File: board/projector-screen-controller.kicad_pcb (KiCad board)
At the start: 2 copper layers, 97.2 x 106 mm, 60 parts, among them J1 ICSP, J2 MSTBVA-3-G, J3 MCV-3-G, J4 MCV-3-G, J5 MCV-3-G, J6 MSTBVA-6-G, J7 MCV-3-G, K1 JS1-12V-F, K2 JS1-12V-F, K3 JS1-12V-F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

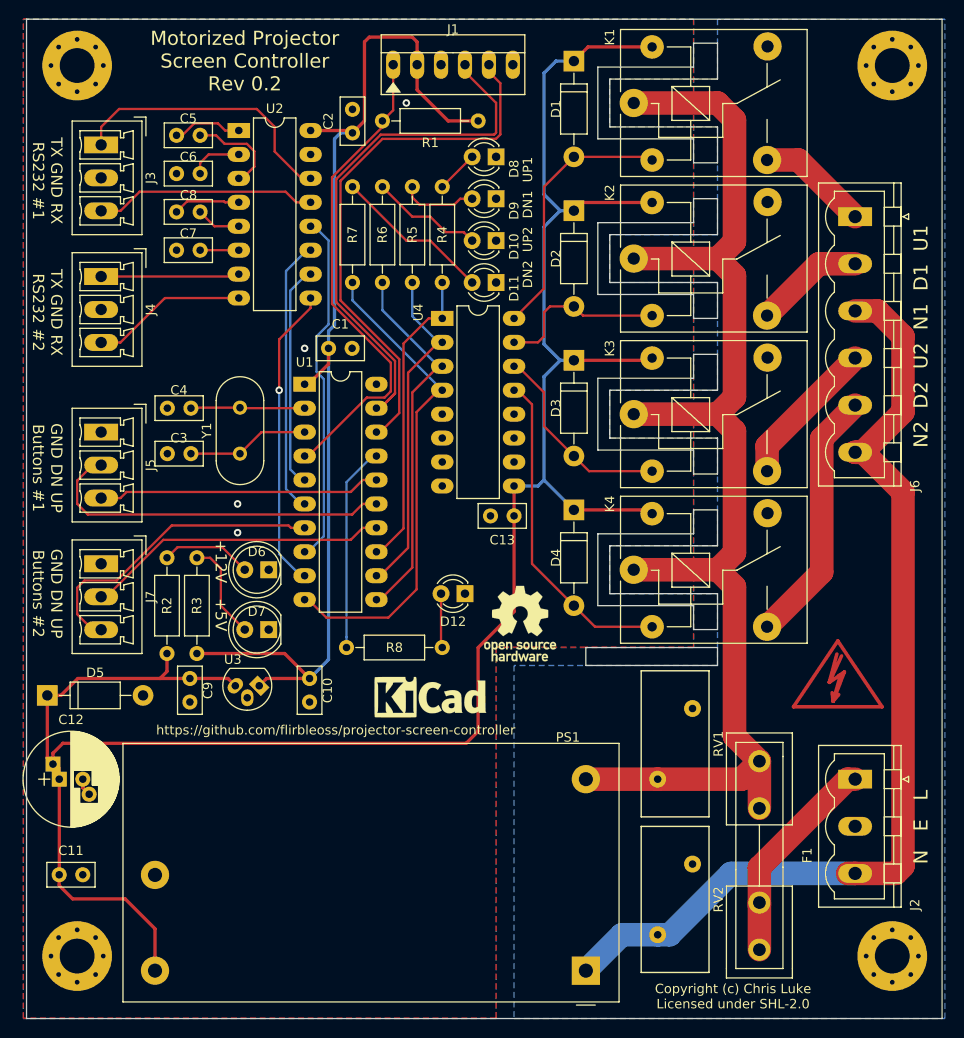
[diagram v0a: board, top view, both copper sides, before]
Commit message: Split the 5v and 12v ground paths
* To control the return path for (noisy) relay current, split the grounds for
  the 12v and 5v sections.
* The grounds are joined by bridges (solder pads) placed adjacent to the 5v
  regulator, on both layers.
* The gound plane is split in two; conveniently the 12v vs 5v components were
  already well placed to make this straightforward.
* 12v power LED uses the 5v ground to simplify routing.
* Add dummy power flags for ERC
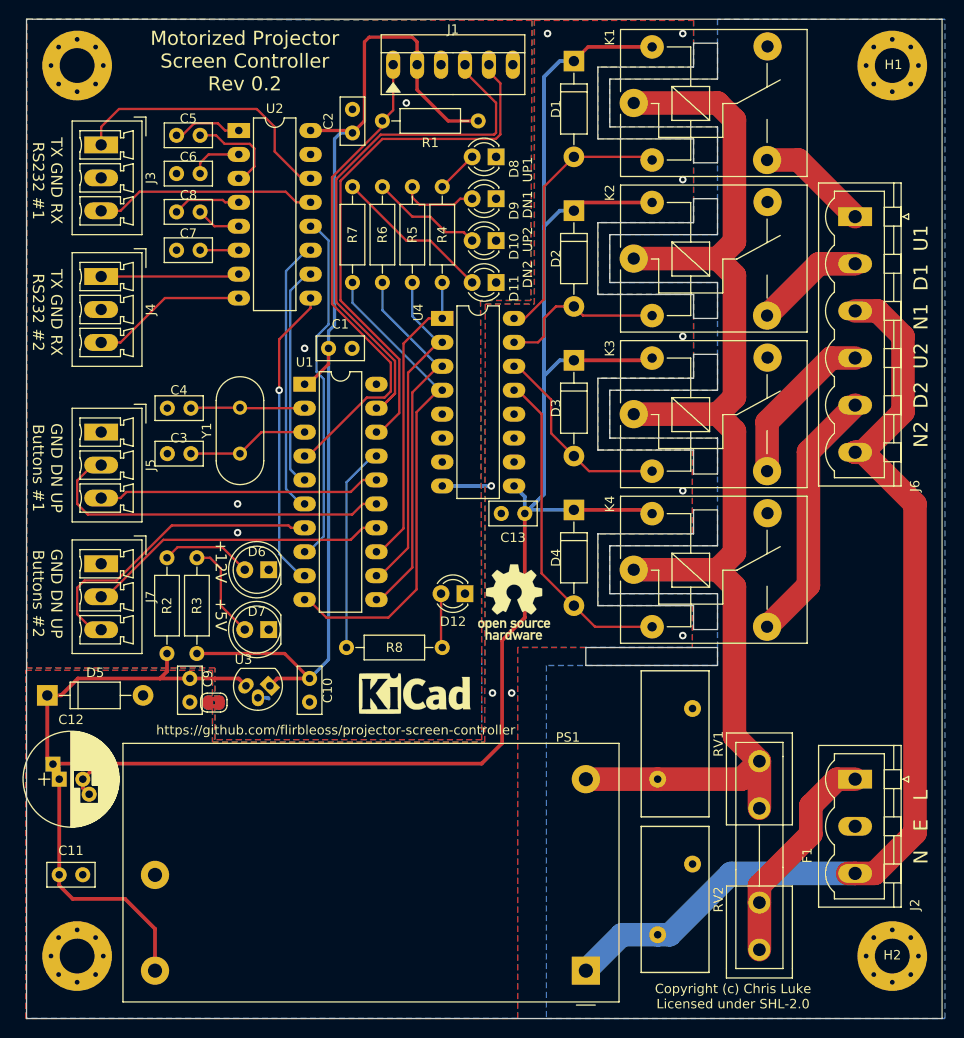
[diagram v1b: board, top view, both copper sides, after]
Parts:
- removed the REF** at (160.7, 115.3)
- removed the REF** at (166.5, 144.5)
- removed the REF** at (166.5, 50.0)
- added H1: MountingHole_Pad, Mounting_Holes:MountingHole_3.7mm_Pad_Via, F.Cu at (166.5, 50.0)
- added H2: MountingHole_Pad, Mounting_Holes:MountingHole_3.7mm_Pad_Via, F.Cu at (166.5, 144.5)
- added JP1: SolderJumper_2_Bridged, Jumper:SolderJumper-2_P1.3mm_Bridged2Bar_RoundedPad1.0x1.5mm, F.Cu at (94.5, 117.6)
- added JP2: SolderJumper_2_Bridged, Jumper:SolderJumper-2_P1.3mm_Bridged2Bar_RoundedPad1.0x1.5mm, B.Cu at (94.5, 117.6)
- moved REF*** 2.37 mm to (126.4, 106.9)
- moved REF** 1.69 mm to (115.8, 116.5)
- moved C13 1.17 mm to (127.5, 97.5)
- moved U3 1.13 mm to (100.5, 115.8)
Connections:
- C11 pad 2: GND -> GNDPWR
- C12 pad 2: GND -> GNDPWR
- C13 pad 2: GND -> GNDPWR
- C9 pad 2: GND -> GNDPWR
- D5 pad 2: GND -> GNDPWR
- PS1 pad 3: GND -> GNDPWR
- U4 pad 8: GND -> GNDPWR
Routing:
- net GNDPWR: track 0.00 -> 8.94 mm, vias 0 -> 9
- net +12V: track 230.7 -> 239.0 mm
- net /Relay/D2_UP_AC: track 15.9 -> 17.4 mm
- net +5V: track 118.0 -> 116.9 mm
- net /MCU/D2_UP_TTL: track 39.9 -> 39.1 mm
- net /MCU/D1_DN_TTL: track 36.4 -> 35.6 mm
- net GND: track 3.68 -> 2.99 mm
- net Net-(D1-Pad2): track 28.2 -> 28.9 mm
- net /MCU/D2_DN_TTL: track 51.8 -> 51.3 mm
- added copper zone on B.Cu, net GNDPWR
- added copper zone on F.Cu, net GNDPWR
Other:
- net class DC 12V added: clearance 0.2, trace_width 0.4, via_dia 0.8, via_drill 0.4
- net class DC 5V added: clearance 0.2, trace_width 0.35, via_dia 1, via_drill 0.5
- net class DC Power removed

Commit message: Add a smattering of ground vias
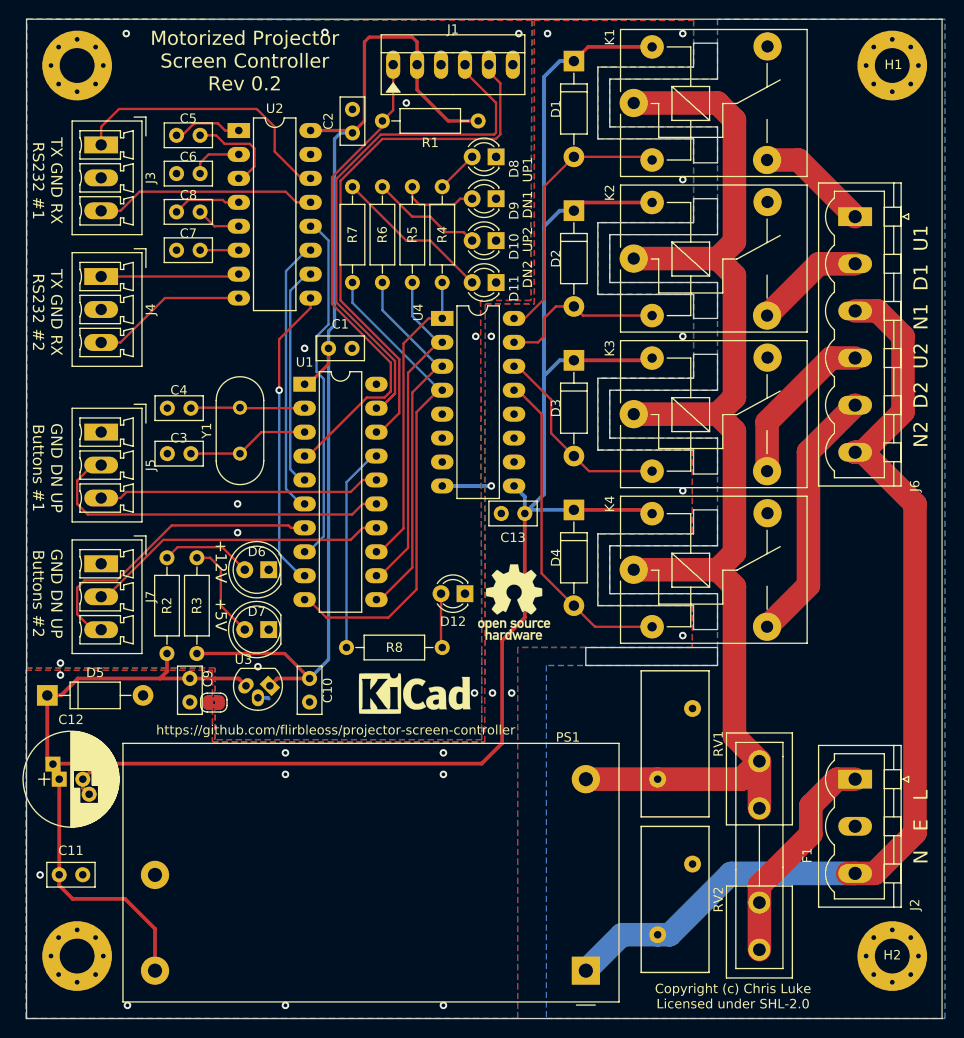
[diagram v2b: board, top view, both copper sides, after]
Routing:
- net GNDPWR: vias 9 -> 20
- net GND: vias 4 -> 11
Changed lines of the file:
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@@
     (thickness 1.6)
     (drawings 76)
-    (tracks 363)
+    (tracks 381)
     (zones 0)
     (modules 61)
@@
   )
   (setup
-    (last_trace_width 0.4)
+    (last_trace_width 0.25)
     (user_trace_width 0.35)
     (user_trace_width 0.4)
@@
   (segment (start 100.237 117.094) (end 100.33 117.187) (width 0.4) (layer B.Cu) (net 2))
   (segment (start 99.187 117.094) (end 100.237 117.094) (width 0.4) (layer B.Cu) (net 2))
+  (via (at 122.301 78.74) (size 0.8) (drill 0.4) (layers F.Cu B.Cu) (net 2))
+  (via (at 126.873 46.609) (size 0.8) (drill 0.4) (layers F.Cu B.Cu) (net 2))
+  (via (at 99.187 113.792) (size 0.8) (drill 0.4) (layers F.Cu B.Cu) (net 2))
+  (via (at 122.174 116.586) (size 0.8) (drill 0.4) (layers F.Cu B.Cu) (net 2))
+  (via (at 78.232 113.411) (size 0.8) (drill 0.4) (layers F.Cu B.Cu) (net 2))
+  (via (at 85.217 46.609) (size 0.8) (drill 0.4) (layers F.Cu B.Cu) (net 2))
+  (via (at 106.299 46.482) (size 0.8) (drill 0.4) (layers F.Cu B.Cu) (net 2))
   (segment (start 99.568 88.9) (end 97.282 91.186) (width 0.25) (layer F.Cu) (net 3) (status 20))
   (segment (start 104.14 88.9) (end 99.568 88.9) (width 0.25) (layer F.Cu) (net 3) (status 10))
@@
   (via (at 124.079 116.586) (size 0.8) (drill 0.4) (layers F.Cu B.Cu) (net 59))
   (via (at 123.952 94.615) (size 0.8) (drill 0.4) (layers F.Cu B.Cu) (net 59))
+  (via (at 102.108 122.936) (size 0.8) (drill 0.4) (layers F.Cu B.Cu) (net 59))
+  (via (at 102.108 125.222) (size 0.8) (drill 0.4) (layers F.Cu B.Cu) (net 59))
+  (via (at 118.872 122.936) (size 0.8) (drill 0.4) (layers F.Cu B.Cu) (net 59))
+  (via (at 118.872 125.222) (size 0.8) (drill 0.4) (layers F.Cu B.Cu) (net 59))
+  (via (at 123.952 78.74) (size 0.8) (drill 0.4) (layers F.Cu B.Cu) (net 59))
+  (via (at 82.55 122.936) (size 0.8) (drill 0.4) (layers F.Cu B.Cu) (net 59))
+  (via (at 78.232 114.681) (size 0.8) (drill 0.4) (layers F.Cu B.Cu) (net 59))
+  (via (at 76.073 135.89) (size 0.8) (drill 0.4) (layers F.Cu B.Cu) (net 59))
+  (via (at 118.872 149.733) (size 0.8) (drill 0.4) (layers F.Cu B.Cu) (net 59))
+  (via (at 102.108 149.733) (size 0.8) (drill 0.4) (layers F.Cu B.Cu) (net 59))
+  (via (at 85.344 149.733) (size 0.8) (drill 0.4) (layers F.Cu B.Cu) (net 59))
   (zone (net 0) (net_name "") (layers F&B.Cu) (hatch edge 0.508)
     (connect_pads (clearance 0.508))

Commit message: Update board symbols, minor ground plane fixes
* Fuse rating, board maximums
* ESD logo
* WEEE logo

* Some ground plane fixes around the MAX232
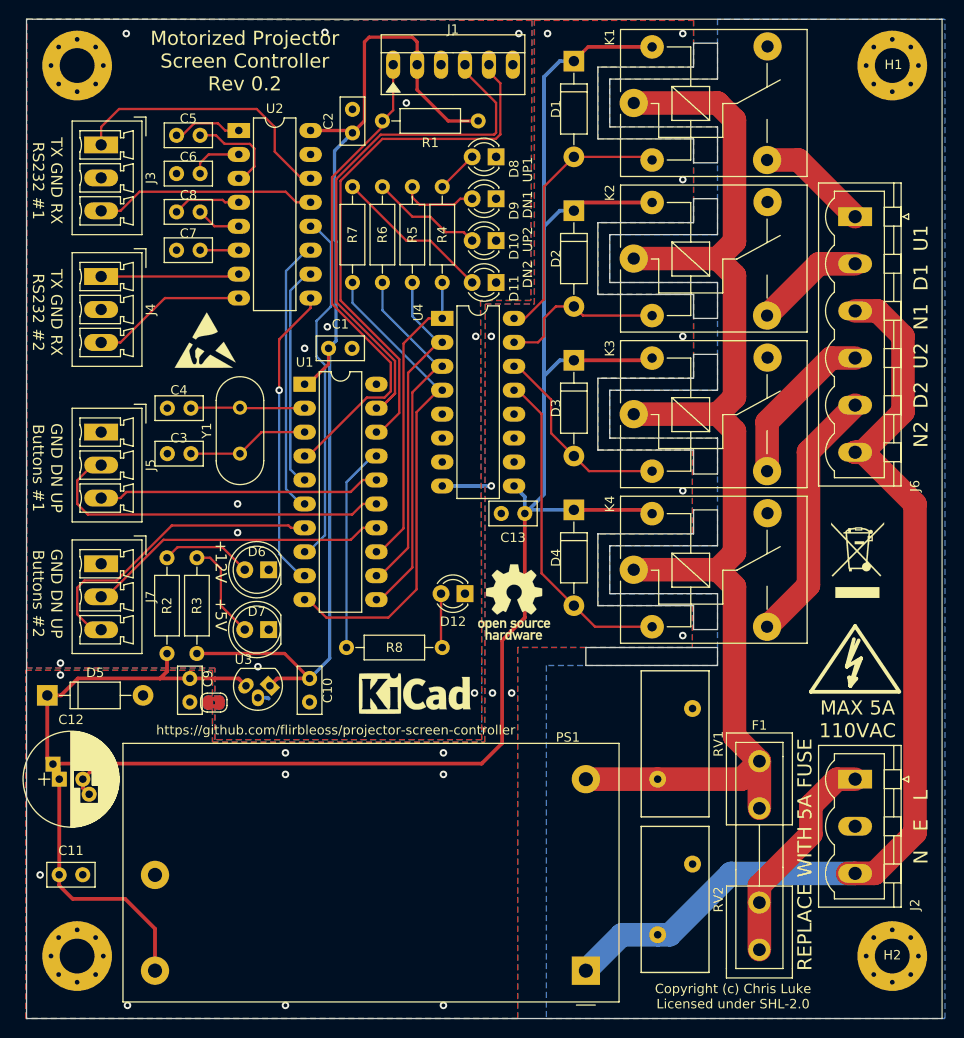
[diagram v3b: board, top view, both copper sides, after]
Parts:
- added REF***: WEEE-Logo_5.6x8mm_SilkScreen, Symbols:WEEE-Logo_5.6x8mm_SilkScreen, F.Cu at (162.8, 102.5)
- added REF***: ESD-Logo_6.6x6mm_SilkScreen, Symbols:ESD-Logo_6.6x6mm_SilkScreen, F.Cu at (93.6, 79.1)
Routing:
- net +5V: track 116.9 -> 116.4 mm
- net GND: vias 11 -> 12
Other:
- board text added: "MAX 5A 110VAC"
- board text added: "REPLACE WITH 5A FUSE"

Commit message: Fix KiCad 4 footprints
* Update the Phoenix connectors with KiCad 5 footprints
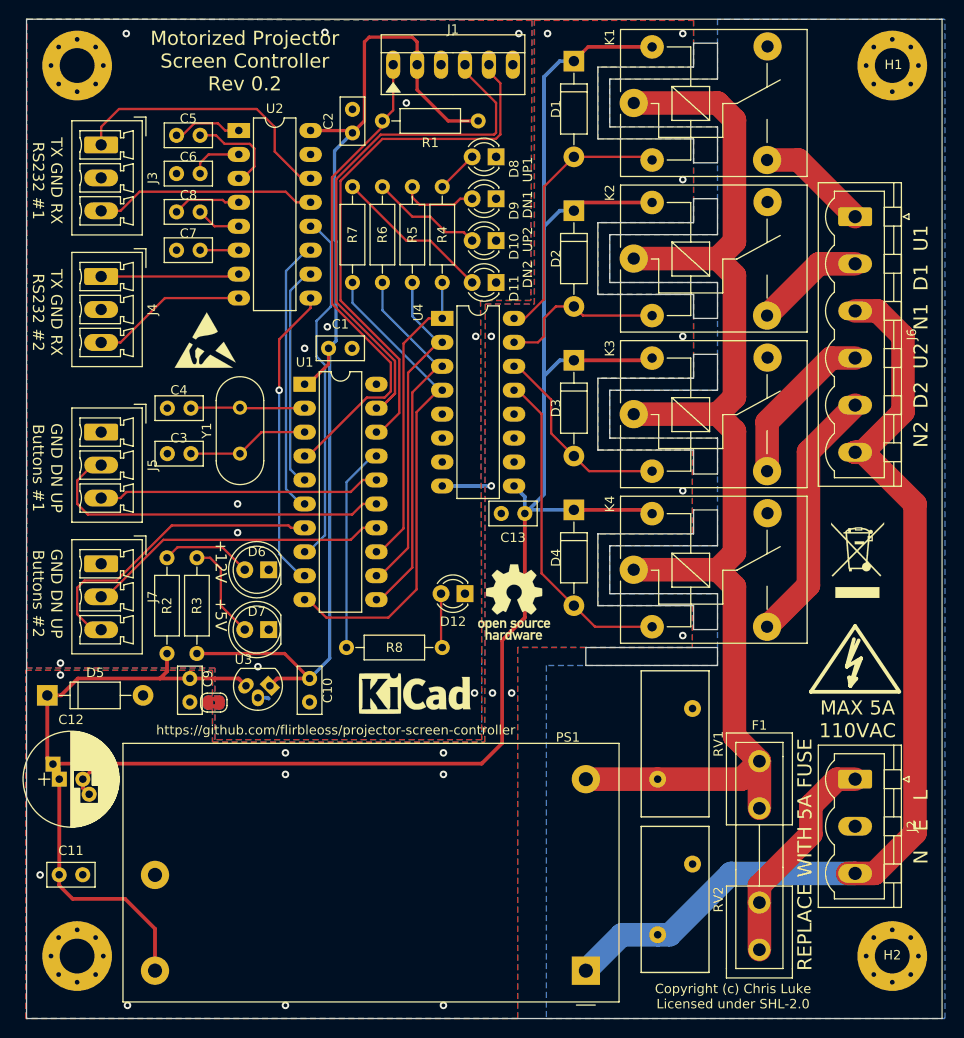
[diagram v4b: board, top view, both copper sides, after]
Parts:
- J2: footprint Connectors_Phoenix:PhoenixContact_MSTBVA-G_03x5.00mm_Vertical -> Connector_Phoenix_MSTB:PhoenixContact_MSTBVA_2,5_3-G_1x03_P5.00mm_Vertical
- J3, J4, J5, J7: footprint Connectors_Phoenix:PhoenixContact_MCV-G_03x3.50mm_Vertical -> Connector_Phoenix_MC:PhoenixContact_MCV_1,5_3-G-3.5_1x03_P3.50mm_Vertical
- J6: footprint Connectors_Phoenix:PhoenixContact_MSTBVA-G_06x5.00mm_Vertical -> Connector_Phoenix_MSTB:PhoenixContact_MSTBVA_2,5_6-G_1x06_P5.00mm_Vertical

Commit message: Update all footprints to KiCad 5 paths
* All footprints updated.
* 3D models for the relays seem to be missing from KiCad, however, so I
  have a copy in my personal library. Mostly cosmetic.
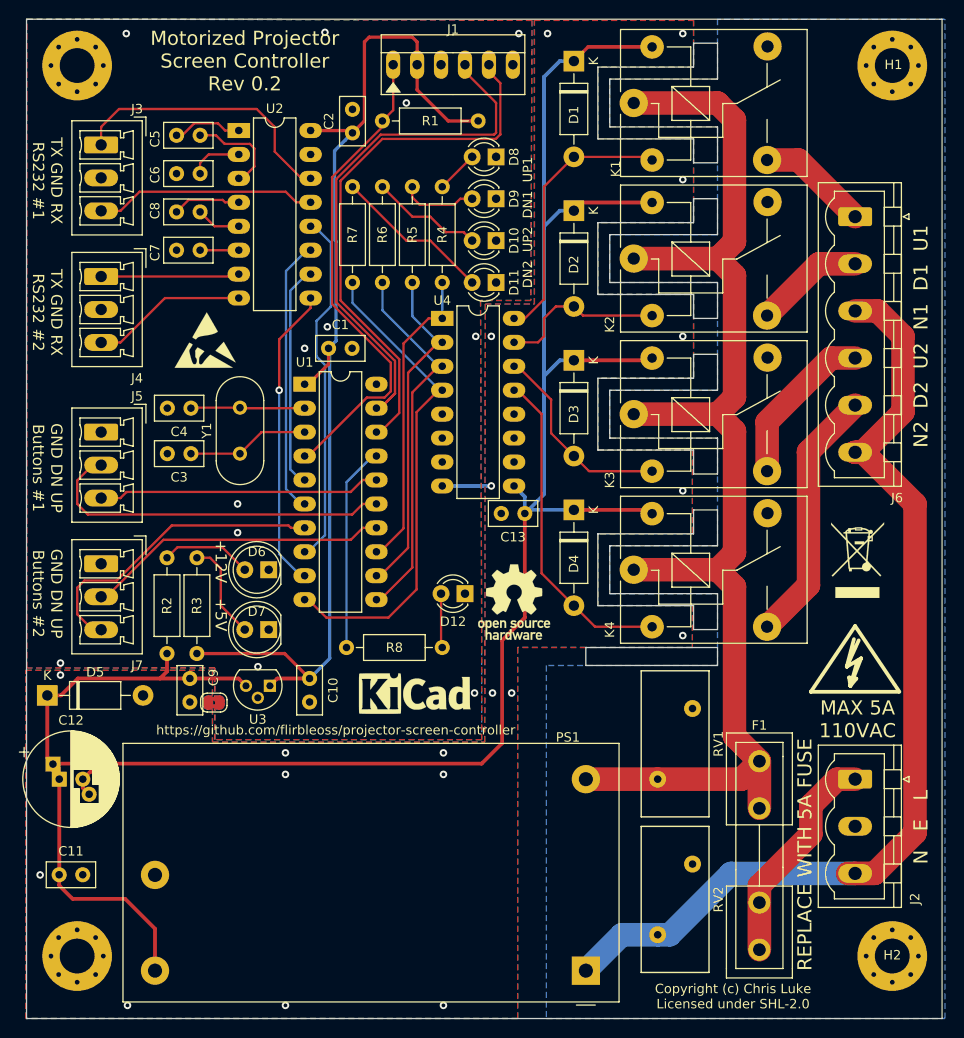
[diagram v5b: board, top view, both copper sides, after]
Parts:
- C1, C10, C11, C13, C2, C3, C4, C5, C6, C7, C8, C9: footprint Capacitors_THT:C_Disc_D5.0mm_W2.5mm_P2.50mm -> Capacitor_THT:C_Disc_D5.0mm_W2.5mm_P2.50mm
- C12: footprint Capacitors_THT:CP_Radial_D10.0mm_P2.50mm_P5.00mm -> Capacitor_THT:CP_Radial_D10.0mm_P2.50mm_P5.00mm
- D1, D2, D3, D4, D5: footprint Diodes_THT:D_DO-41_SOD81_P10.16mm_Horizontal -> Diode_THT:D_DO-41_SOD81_P10.16mm_Horizontal
- D10, D11, D12, D8, D9: footprint LEDs:LED_D3.0mm -> LED_THT:LED_D3.0mm
- D6, D7: footprint LEDs:LED_D5.0mm -> LED_THT:LED_D5.0mm
- K1, K2, K3, K4: footprint Relays_THT:Relay_SPDT_SANYOU_SRD_Series_Form_C -> Relay_THT:Relay_SPDT_SANYOU_SRD_Series_Form_C
- R1, R2, R3, R4, R5, R6, R7, R8: footprint Resistors_THT:R_Axial_DIN0207_L6.3mm_D2.5mm_P10.16mm_Horizontal -> Resistor_THT:R_Axial_DIN0207_L6.3mm_D2.5mm_P10.16mm_Horizontal
- U1: footprint Housings_DIP:DIP-20_W7.62mm_LongPads -> Package_DIP:DIP-20_W7.62mm_LongPads
- U2, U4: footprint Housings_DIP:DIP-16_W7.62mm_LongPads -> Package_DIP:DIP-16_W7.62mm_LongPads
- U3: footprint TO_SOT_Packages_THT:TO-92_Molded_Narrow_Oval -> Package_TO_SOT_THT:TO-92L
- Y1: footprint Crystals:Crystal_HC49-4H_Vertical -> Crystal:Crystal_HC49-4H_Vertical
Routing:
- net GND: track 2.99 -> 1.81 mm
